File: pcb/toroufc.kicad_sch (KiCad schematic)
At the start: 67 parts, among them J1 Conn_01x16_Male, J10 USB_B_Mini, J2 Conn_01x16_Male, J3 Conn_01x16_Male, J4 Conn_01x16_Male, J5 Conn_01x16_Male, J6 Conn_01x16_Male, J7 Conn_01x16_Male, J8 Conn_01x09_Male, J9 Conn_01x09_Male, U1 YAAJ_BluePill

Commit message: More tidying up.
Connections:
- net POT1: now also U1.25 (PA0); no longer U1.30 (PA5)
- net POT2: now also U1.26 (PA1); no longer U1.29 (PA4)
- net POT3: now also U1.27 (PA2); no longer U1.28 (PA3)
- net POT4: now also U1.28 (PA3); no longer U1.27 (PA2)
- net POT5: now also U1.29 (PA4); no longer U1.26 (PA1)
- net POT6: now also U1.30 (PA5); no longer U1.25 (PA0)
- net VCC: now also U1.20 (3V3), U1.38 (3V3); no longer J10.1 (VBUS), U1.18 (5V)
- net REN2SW: now reaches U1.23 (PC14)
- net REN1SW: now reaches U1.24 (PC15)
- new net Vusb: J10.1 (VBUS), U1.18 (5V)
- no-connect marks 0 -> 5
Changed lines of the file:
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@@
   (junction (at 401.32 113.538) (diameter 0) (color 0 0 0 0)
   )
+  (junction (at 305.308 87.884) (diameter 0) (color 0 0 0 0)
+  )
   (junction (at 250.19 185.42) (diameter 0) (color 0 0 0 0)
   )
@@
   (junction (at 321.31 205.74) (diameter 0) (color 0 0 0 0)
   )
+  (no_connect (at 324.358 133.604))
+  (no_connect (at 324.358 95.504))
+  (no_connect (at 298.958 87.884))
+  (no_connect (at 219.71 122.428))
+  (no_connect (at 209.55 127.508))
   (wire (pts (xy 224.79 182.88) (xy 224.79 189.23))
     (stroke (width 0) (type default) (color 0 0 0 0))
@@
     (stroke (width 0) (type default) (color 0 0 0 0))
   )
+  (wire (pts (xy 305.308 87.884) (xy 306.578 87.884))
+    (stroke (width 0) (type default) (color 0 0 0 0))
+  )
   (wire (pts (xy 288.29 196.85) (xy 288.29 201.93))
     (stroke (width 0) (type default) (color 0 0 0 0))
@@
     (stroke (width 0) (type default) (color 0 0 0 0))
   )
-  (wire (pts (xy 301.498 76.962) (xy 301.498 87.884))
-    (stroke (width 0) (type default) (color 0 0 0 0))
-  )
   (wire (pts (xy 369.57 205.74) (xy 369.57 196.85))
     (stroke (width 0) (type default) (color 0 0 0 0))
@@
     (stroke (width 0) (type default) (color 0 0 0 0))
   )
+  (wire (pts (xy 305.308 87.884) (xy 305.308 79.756))
+    (stroke (width 0) (type default) (color 0 0 0 0))
+  )
   (wire (pts (xy 398.78 111.76) (xy 398.78 116.332))
     (stroke (width 0) (type default) (color 0 0 0 0))
@@
     (stroke (width 0) (type default) (color 0 0 0 0))
   )
+  (wire (pts (xy 324.358 131.064) (xy 338.074 131.064))
+    (stroke (width 0) (type default) (color 0 0 0 0))
+  )
   (wire (pts (xy 331.47 182.88) (xy 331.47 189.23))
     (stroke (width 0) (type default) (color 0 0 0 0))
@@
     (stroke (width 0) (type default) (color 0 0 0 0))
   )
+  (wire (pts (xy 301.498 87.884) (xy 301.498 77.724))
+    (stroke (width 0) (type default) (color 0 0 0 0))
+  )
   (wire (pts (xy 168.91 185.42) (xy 173.99 185.42))
     (stroke (width 0) (type default) (color 0 0 0 0))
@@
     (stroke (width 0) (type default) (color 0 0 0 0))
   )
+  (wire (pts (xy 324.358 128.524) (xy 338.074 128.524))
+    (stroke (width 0) (type default) (color 0 0 0 0))
+  )
   (wire (pts (xy 148.336 205.74) (xy 148.336 200.66))
     (stroke (width 0) (type default) (color 0 0 0 0))
@@
     (stroke (width 0) (type default) (color 0 0 0 0))
   )
+  (wire (pts (xy 304.038 87.884) (xy 305.308 87.884))
+    (stroke (width 0) (type default) (color 0 0 0 0))
+  )
   (wire (pts (xy 401.32 113.538) (xy 393.7 113.538))
     (stroke (width 0) (type default) (color 0 0 0 0))
@@
     (effects (font (size 1.27 1.27)) (justify left bottom))
   )
+  (label "Vusb" (at 228.092 105.918 180)
+    (effects (font (size 1.27 1.27)) (justify right bottom))
+  )
   (label "COL5" (at 269.748 110.744 0)
     (effects (font (size 1.27 1.27)) (justify left bottom))
   )
+  (label "REN1SW" (at 338.074 128.524 0)
+    (effects (font (size 1.27 1.27)) (justify left bottom))
+  )
+  (label "REN2SW" (at 338.074 131.064 0)
+    (effects (font (size 1.27 1.27)) (justify left bottom))
+  )
   (label "COL2" (at 132.842 167.894 0)
     (effects (font (size 1.27 1.27)) (justify left bottom))
   )
-  (label "POT5" (at 338.328 123.444 0)
+  (label "POT2" (at 338.328 123.444 0)
     (effects (font (size 1.27 1.27)) (justify left bottom))
   )
-  (label "POT1" (at 338.328 113.284 0)
+  (label "POT6" (at 338.328 113.284 0)
     (effects (font (size 1.27 1.27)) (justify left bottom))
   )
@@
     (effects (font (size 1.27 1.27)) (justify left bottom))
   )
-  (label "POT2" (at 338.328 115.824 0)
+  (label "POT5" (at 338.328 115.824 0)
     (effects (font (size 1.27 1.27)) (justify left bottom))
   )
@@
     (effects (font (size 1.27 1.27)) (justify left bottom))
   )
-  (label "POT6" (at 338.328 125.984 0)
+  (label "POT1" (at 338.328 125.984 0)
     (effects (font (size 1.27 1.27)) (justify left bottom))
   )
@@
     (effects (font (size 1.27 1.27)) (justify left bottom))
   )
-  (label "POT4" (at 338.328 120.904 0)
+  (label "Vusb" (at 301.498 77.724 180)
+    (effects (font (size 1.27 1.27)) (justify right bottom))
+  )
+  (label "POT3" (at 338.328 120.904 0)
     (effects (font (size 1.27 1.27)) (justify left bottom))
   )
@@
     (effects (font (size 1.27 1.27)) (justify left bottom))
   )
-  (label "POT3" (at 338.328 118.364 0)
+  (label "POT4" (at 338.328 118.364 0)
     (effects (font (size 1.27 1.27)) (justify left bottom))
   )
@@
     (pin "2")
   )
-  (symbol (lib_id "power:VCC") (at 301.498 76.962 0) (unit 1)
+  (symbol (lib_id "power:VCC") (at 305.308 79.756 0) (unit 1)
     (in_bom yes) (on_board yes) (fields_autoplaced)
-    (property "Reference" "#PWR?" (id 0) (at 301.498 80.772 0)
+    (property "Reference" "#PWR?" (id 0) (at 305.308 83.566 0)
       (effects (font (size 1.27 1.27)) hide)
     )
-    (property "Value" "VCC" (id 1) (at 301.498 72.136 0))
-    (property "Footprint" "" (id 2) (at 301.498 76.962 0)
+    (property "Value" "VCC" (id 1) (at 305.308 74.93 0))
+    (property "Footprint" "" (id 2) (at 305.308 79.756 0)
       (effects (font (size 1.27 1.27)) hide)
     )
-    (property "Datasheet" "" (id 3) (at 301.498 76.962 0)
+    (property "Datasheet" "" (id 3) (at 305.308 79.756 0)
       (effects (font (size 1.27 1.27)) hide)
     )
@@
     (pin "1")
   )
-  (symbol (lib_id "power:VCC") (at 228.092 105.918 0) (unit 1)
-    (in_bom yes) (on_board yes) (fields_autoplaced)
-    (property "Reference" "#PWR?" (id 0) (at 228.092 109.728 0)
-      (effects (font (size 1.27 1.27)) hide)
-    )
-    (property "Value" "VCC" (id 1) (at 228.092 101.092 0))
-    (property "Footprint" "" (id 2) (at 228.092 105.918 0)
-      (effects (font (size 1.27 1.27)) hide)
-    )
-    (property "Datasheet" "" (id 3) (at 228.092 105.918 0)
-      (effects (font (size 1.27 1.27)) hide)
-    )
-    (pin "1")
-  )
   (symbol (lib_id "power:VCC") (at 372.618 108.966 0) (unit 1)
     (in_bom yes) (on_board yes) (fields_autoplaced)
@@
       (reference "#PWR?") (unit 1) (value "GND") (footprint "")
     )
-    (path "/dde93976-757c-4038-872b-0c5b704c5a92"
-      (reference "#PWR?") (unit 1) (value "VCC") (footprint "")
-    )
     (path "/e41f886c-3ec0-46eb-8123-dceb7f5fc8e6"

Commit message: Starting with the PCB.
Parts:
- removed D23, D24, D25, D26, D27, D28, D29, D30, D31, D32, D33, D34, D35, D36, D37, D38, D39, D40, D41, D42, D43, D44, D45, D46, D47, D48, D49, D50, D51, D52, D53, D54, D55, D56: D, Diode_SMD:D_SOD-123, symbol Device:D
- removed J1, J2, J3, J4, J5, J6, J7: Conn_01x16_Male, Connector_PinHeader_2.54mm:PinHeader_1x16_P2.54mm_Vertical, symbol Connector:Conn_01x16_Male
- added J1: HAT, Connector_PinHeader_2.54mm:PinHeader_1x06_P2.54mm_Vertical, symbol Connector:Conn_01x06_Male
- added J10: RPAD, Connector_PinHeader_2.54mm:PinHeader_1x06_P2.54mm_Vertical, symbol Connector:Conn_01x06_Male
- added J13: REN1, Connector_PinHeader_2.54mm:PinHeader_1x05_P2.54mm_Vertical, symbol Connector:Conn_01x05_Male
- added J14: REN2, Connector_PinHeader_2.54mm:PinHeader_1x05_P2.54mm_Vertical, symbol Connector:Conn_01x05_Male
- added J15: I2C, Connector_PinHeader_2.54mm:PinHeader_1x04_P2.54mm_Vertical, symbol Connector:Conn_01x04_Male
- added J2: RKR1-2, Connector_PinHeader_2.54mm:PinHeader_1x06_P2.54mm_Vertical, symbol Connector:Conn_01x06_Male
- added J3: RKR3-4, Connector_PinHeader_2.54mm:PinHeader_1x06_P2.54mm_Vertical, symbol Connector:Conn_01x06_Male
- added J4: LVR1-2, Connector_PinHeader_2.54mm:PinHeader_1x06_P2.54mm_Vertical, symbol Connector:Conn_01x06_Male
- added J5: MASTER-BIG1, Connector_PinHeader_2.54mm:PinHeader_1x06_P2.54mm_Vertical, symbol Connector:Conn_01x06_Male
- added J6: BIG2-3-4, Connector_PinHeader_2.54mm:PinHeader_1x06_P2.54mm_Vertical, symbol Connector:Conn_01x06_Male
- added J7: NPAD, Connector_PinHeader_2.54mm:PinHeader_1x10_P2.54mm_Vertical, symbol Connector:Conn_01x10_Male
- added J8: HPAD, Connector_PinHeader_2.54mm:PinHeader_1x08_P2.54mm_Vertical, symbol Connector:Conn_01x08_Male
- added J9: LPAD, Connector_PinHeader_2.54mm:PinHeader_1x06_P2.54mm_Vertical, symbol Connector:Conn_01x06_Male
- J11: renamed from J8; value Conn_01x09_Male -> POT1-3; footprint (none) -> Connector_PinHeader_2.54mm:PinHeader_1x09_P2.54mm_Vertical
- J12: renamed from J9; value Conn_01x09_Male -> POT4-6; footprint (none) -> Connector_PinHeader_2.54mm:PinHeader_1x09_P2.54mm_Vertical
- J16: renamed from J10; footprint (none) -> Connector_USB:USB_Mini-B_Wuerth_65100516121_Horizontal
- U1: value YAAJ_BluePill -> BluePill
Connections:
- net COL1: now also J8.1 (Pin_1)
- net COL2: now also J7.1 (Pin_1)
- net COL3: now also J5.5 (Pin_5), J6.1 (Pin_1), J6.3 (Pin_3), J6.5 (Pin_5), J7.2 (Pin_2)
- net COL4: now also J9.1 (Pin_1)
- net COL5: now also J10.1 (Pin_1), J5.1 (Pin_1), J5.3 (Pin_3)
- net COL6: now also J2.1 (Pin_1), J2.4 (Pin_4), J3.1 (Pin_1), J3.4 (Pin_4)
- net COL7: now also J1.1 (Pin_1), J4.1 (Pin_1), J4.4 (Pin_4)
- net GND: now also J13.5 (Pin_5), J14.5 (Pin_5), J15.4 (Pin_4)
- net POT1: now also U1.27 (PA2); no longer U1.25 (PA0)
- net POT3: now also U1.25 (PA0); no longer U1.27 (PA2)
- net REN1C: now also U1.1 (PB12), J13.1 (Pin_1); no longer U1.2 (PB13)
- net REN1D: now also U1.2 (PB13), J13.2 (Pin_2); no longer U1.1 (PB12)
- net REN1SW: now also J13.3 (Pin_3)
- net REN2C: now also U1.3 (PB14), J14.1 (Pin_1); no longer U1.4 (PB15)
- net REN2D: now also U1.4 (PB15), J14.2 (Pin_2); no longer U1.3 (PB14)
- net REN2SW: now also J14.3 (Pin_3)
- net ROW1: now also D13.1 (K), D5.1 (K), J10.2 (Pin_2), J7.3 (Pin_3), J8.2 (Pin_2), J9.2 (Pin_2); no longer D16.1 (K), D8.1 (K)
- net ROW2: now also D14.1 (K), D6.1 (K), J10.3 (Pin_3), J7.4 (Pin_4), J8.3 (Pin_3), J9.3 (Pin_3); no longer D15.1 (K), D7.1 (K)
- net ROW3: now also D15.1 (K), D7.1 (K), J10.4 (Pin_4), J7.5 (Pin_5), J8.4 (Pin_4), J9.4 (Pin_4); no longer D14.1 (K), D22.1 (K), D6.1 (K)
- net ROW4: now also D16.1 (K), D19.1 (K), D8.1 (K), J10.5 (Pin_5), J7.6 (Pin_6), J8.5 (Pin_5), J9.5 (Pin_5); no longer D13.1 (K), D21.1 (K), D5.1 (K)
- net ROW5: now also D1.1 (K), D9.1 (K), J10.6 (Pin_6), J7.7 (Pin_7), J8.6 (Pin_6), J9.6 (Pin_6); no longer D12.1 (K), D4.1 (K)
- net ROW6: now also D10.1 (K), D17.1 (K), D2.1 (K), D21.1 (K), J7.8 (Pin_8), J8.7 (Pin_7); no longer D11.1 (K), D19.1 (K), D3.1 (K)
- net ROW7: now also D11.1 (K), D22.1 (K), D3.1 (K), J7.9 (Pin_9), J8.8 (Pin_8); no longer D10.1 (K), D2.1 (K)
- net ROW8: now also D12.1 (K), D4.1 (K), J7.10 (Pin_10); no longer D1.1 (K), D17.1 (K), D9.1 (K)
- net SCL: now also J15.2 (Pin_2)
- net SDA: now also J15.3 (Pin_3)
- net VCC: now also J13.4 (Pin_4), J14.4 (Pin_4), J15.1 (Pin_1)
- net at D8.2 (A): now also J2.6 (Pin_6)
- net at D3.2 (A): now also J1.4 (Pin_4)
- net at D2.2 (A): now also J1.3 (Pin_3)
- net at D1.2 (A): now also J1.2 (Pin_2)
- net at D7.2 (A): now also J2.5 (Pin_5)
- net at D6.2 (A): now also J2.3 (Pin_3)
- net at D5.2 (A): now also J2.2 (Pin_2)
- net at D4.2 (A): now also J1.5 (Pin_5)
- net at D16.2 (A): now also J4.6 (Pin_6)
- net at D11.2 (A): now also J3.5 (Pin_5)
- net at D10.2 (A): now also J3.3 (Pin_3)
- net at D9.2 (A): now also J3.2 (Pin_2)
- net at D15.2 (A): now also J4.5 (Pin_5)
- net at D14.2 (A): now also J4.3 (Pin_3)
- net at D13.2 (A): now also J4.2 (Pin_2)
- net at D12.2 (A): now also J3.6 (Pin_6)
- net at D19.2 (A): now also J5.6 (Pin_6)
- net at D18.2 (A): now also J5.4 (Pin_4)
- net at D17.2 (A): now also J5.2 (Pin_2)
- net at D22.2 (A): now also J6.6 (Pin_6)
- net at D21.2 (A): now also J6.4 (Pin_4)
- net at D20.2 (A): now also J6.2 (Pin_2)
- no-connect marks 5 -> 6
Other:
- moved on the sheet: D1, D2, D3, D4, D5, D6, D7, D8, J11, J12, J16, U1

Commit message: First PCB that passes DRC
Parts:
- removed J16: USB_B_Mini, Connector_USB:USB_Mini-B_Wuerth_65100516121_Horizontal, symbol Connector:USB_B_Mini
- added J16: Conn_01x04_Male, Connector_PinHeader_2.54mm:PinHeader_1x04_P2.54mm_Vertical, symbol Connector:Conn_01x04_Male
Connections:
- net GND: now also J16.2 (Pin_2)
- net ROW1: now also U1.36 (PB11); no longer U1.31 (PA6)
- net ROW2: now also U1.35 (PB10); no longer U1.32 (PA7)
- net ROW3: now also U1.34 (PB1); no longer U1.33 (PB0)
- net ROW4: now also U1.33 (PB0); no longer D19.1 (K), U1.34 (PB1)
- net ROW5: now also D19.1 (K), U1.31 (PA6); no longer D20.1 (K), U1.35 (PB10)
- net ROW6: now also D20.1 (K), U1.32 (PA7); no longer D21.1 (K), U1.36 (PB11)
- net ROW7: now also D21.1 (K); no longer D22.1 (K)
- net ROW8: now also D22.1 (K)
- net SCL: now also J15.3 (Pin_3); no longer J15.2 (Pin_2)
- net SDA: now also J15.2 (Pin_2); no longer J15.3 (Pin_3)
- net USBD+: now also J16.4 (Pin_4)
- net USBD-: now also J16.3 (Pin_3)
- net Vusb: now also J16.1 (Pin_1)
- no-connect marks 6 -> 4

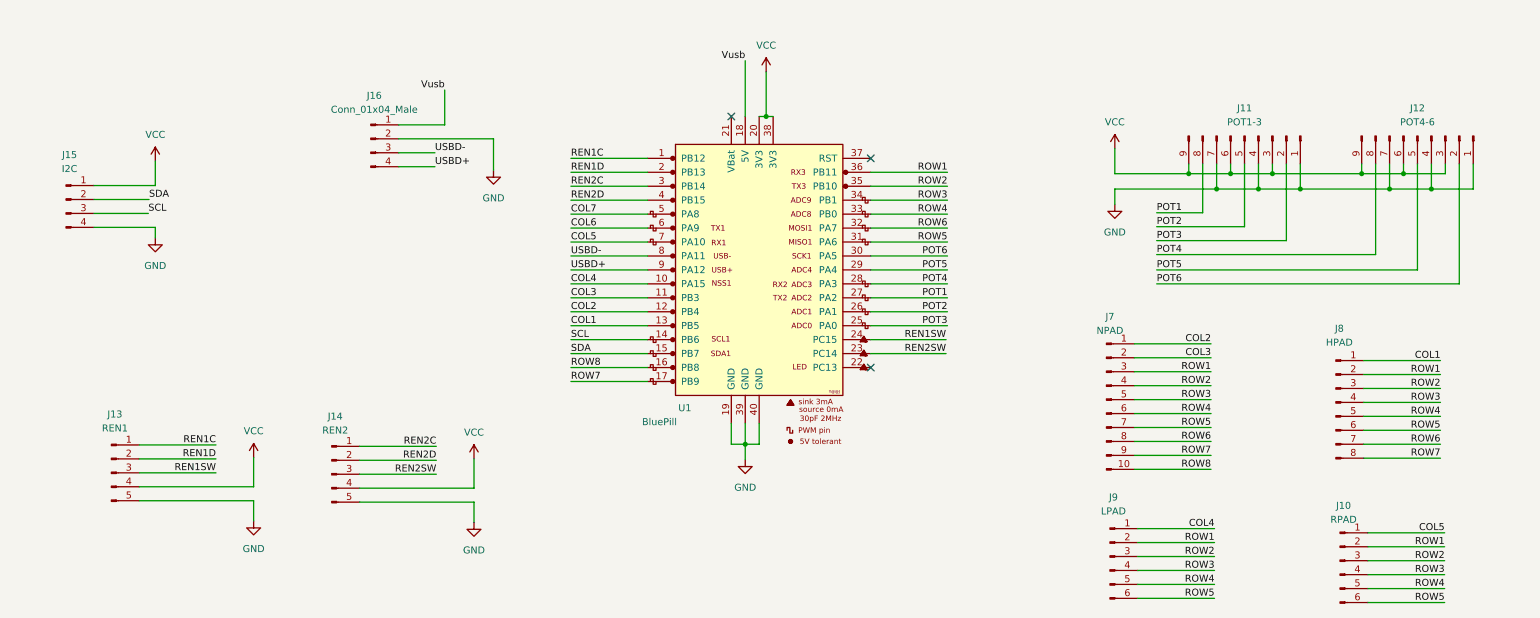
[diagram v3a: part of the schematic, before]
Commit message: Changing pcb connectors to JST XH
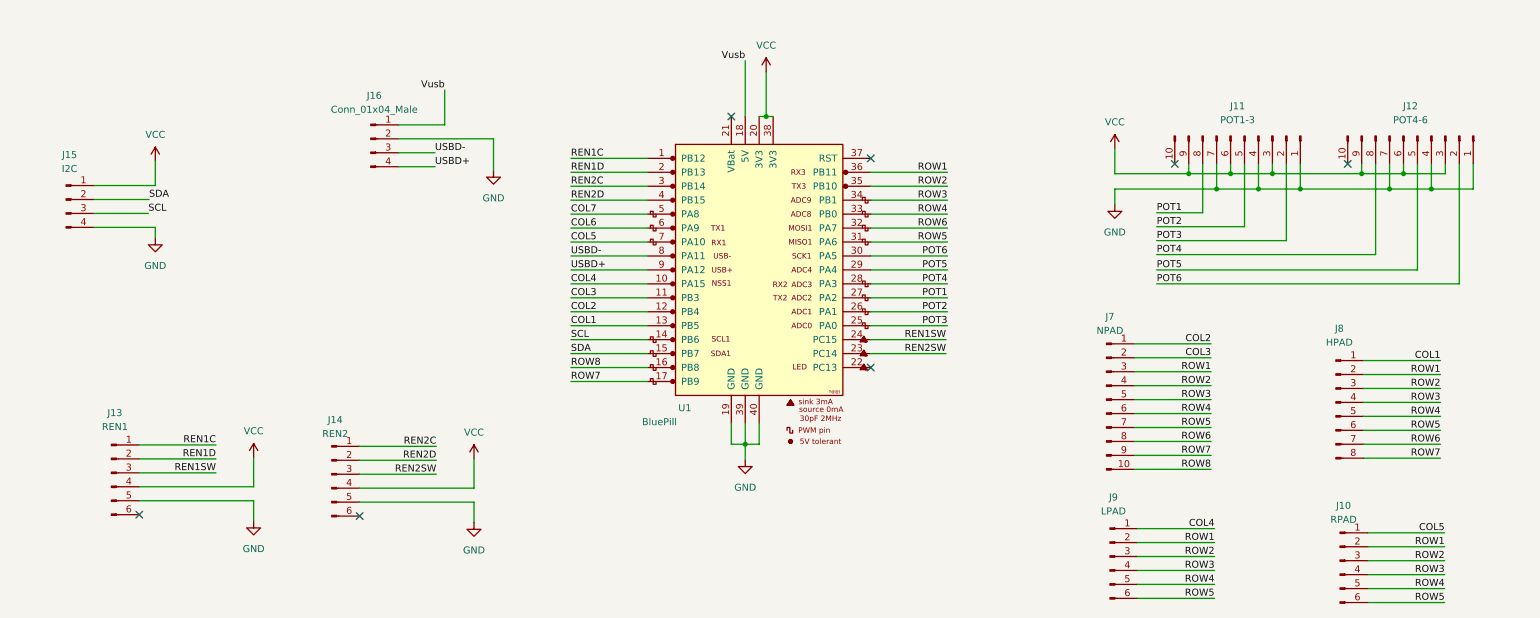
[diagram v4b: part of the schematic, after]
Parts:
- removed J11: POT1-3, Connector_PinHeader_2.54mm:PinHeader_1x09_P2.54mm_Vertical, symbol Connector:Conn_01x09_Male
- removed J12: POT4-6, Connector_PinHeader_2.54mm:PinHeader_1x09_P2.54mm_Vertical, symbol Connector:Conn_01x09_Male
- removed J13: REN1, Connector_PinHeader_2.54mm:PinHeader_1x05_P2.54mm_Vertical, symbol Connector:Conn_01x05_Male
- removed J14: REN2, Connector_PinHeader_2.54mm:PinHeader_1x05_P2.54mm_Vertical, symbol Connector:Conn_01x05_Male
- added J11: POT1-3, Connector_JST:JST_XH_B10B-XH-A_1x10_P2.50mm_Vertical, symbol Connector:Conn_01x10_Male
- added J12: POT4-6, Connector_JST:JST_XH_B10B-XH-A_1x10_P2.50mm_Vertical, symbol Connector:Conn_01x10_Male
- added J13: REN1, Connector_JST:JST_XH_B6B-XH-A_1x06_P2.50mm_Vertical, symbol Connector:Conn_01x06_Male
- added J14: REN2, Connector_JST:JST_XH_B6B-XH-A_1x06_P2.50mm_Vertical, symbol Connector:Conn_01x06_Male
- J1, J10, J2, J3, J4, J5, J6, J9: footprint Connector_PinHeader_2.54mm:PinHeader_1x06_P2.54mm_Vertical -> Connector_JST:JST_XH_B6B-XH-A_1x06_P2.50mm_Vertical
- J15, J16: footprint Connector_PinHeader_2.54mm:PinHeader_1x04_P2.54mm_Vertical -> Connector_JST:JST_XH_B4B-XH-A_1x04_P2.50mm_Vertical
- J7: footprint Connector_PinHeader_2.54mm:PinHeader_1x10_P2.54mm_Vertical -> Connector_JST:JST_XH_B10B-XH-A_1x10_P2.50mm_Vertical
- J8: footprint Connector_PinHeader_2.54mm:PinHeader_1x08_P2.54mm_Vertical -> Connector_JST:JST_XH_B8B-XH-A_1x08_P2.50mm_Vertical
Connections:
- net GND: now also J11.1 (Pin_1), J11.4 (Pin_4), J11.7 (Pin_7), J12.1 (Pin_1), J12.4 (Pin_4), J12.7 (Pin_7), J13.5 (Pin_5), J14.5 (Pin_5)
- net POT1: now also J11.8 (Pin_8)
- net POT2: now also J11.5 (Pin_5)
- net POT3: now also J11.2 (Pin_2)
- net POT4: now also J12.8 (Pin_8)
- net POT5: now also J12.5 (Pin_5)
- net POT6: now also J12.2 (Pin_2)
- net REN1C: now also J13.1 (Pin_1)
- net REN1D: now also J13.2 (Pin_2)
- net REN1SW: now also J13.3 (Pin_3)
- net REN2C: now also J14.1 (Pin_1)
- net REN2D: now also J14.2 (Pin_2)
- net REN2SW: now also J14.3 (Pin_3)
- net VCC: now also J11.3 (Pin_3), J11.6 (Pin_6), J11.9 (Pin_9), J12.3 (Pin_3), J12.6 (Pin_6), J12.9 (Pin_9), J13.4 (Pin_4), J14.4 (Pin_4)
- no-connect marks 4 -> 8

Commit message: Fixing some lanes.
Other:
- moved on the sheet: D1, D10, D11, D12, D13, D14, D15, D16, D17, D18, D19, D2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
